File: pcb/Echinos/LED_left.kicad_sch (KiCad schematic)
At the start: 9 parts

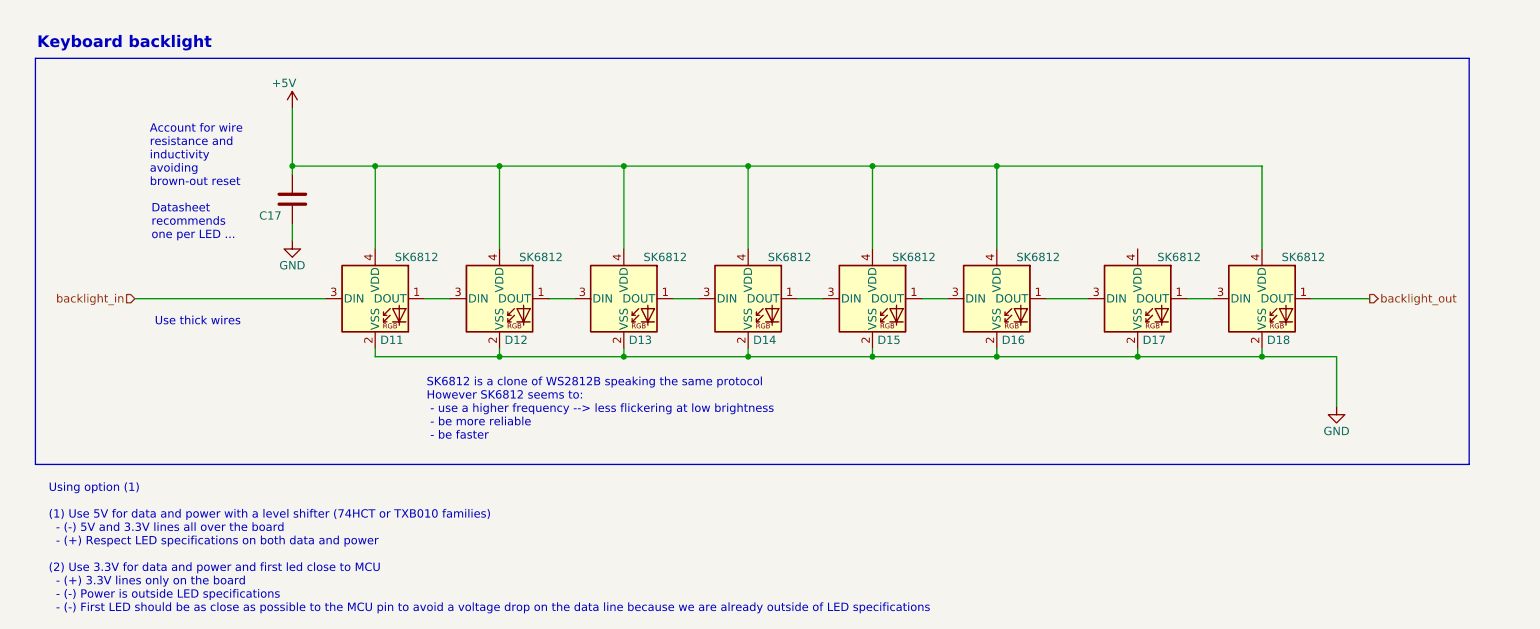
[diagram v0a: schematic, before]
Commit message: [PCB] - Save last state with Helios MCU board and gasket tabs on PCB.
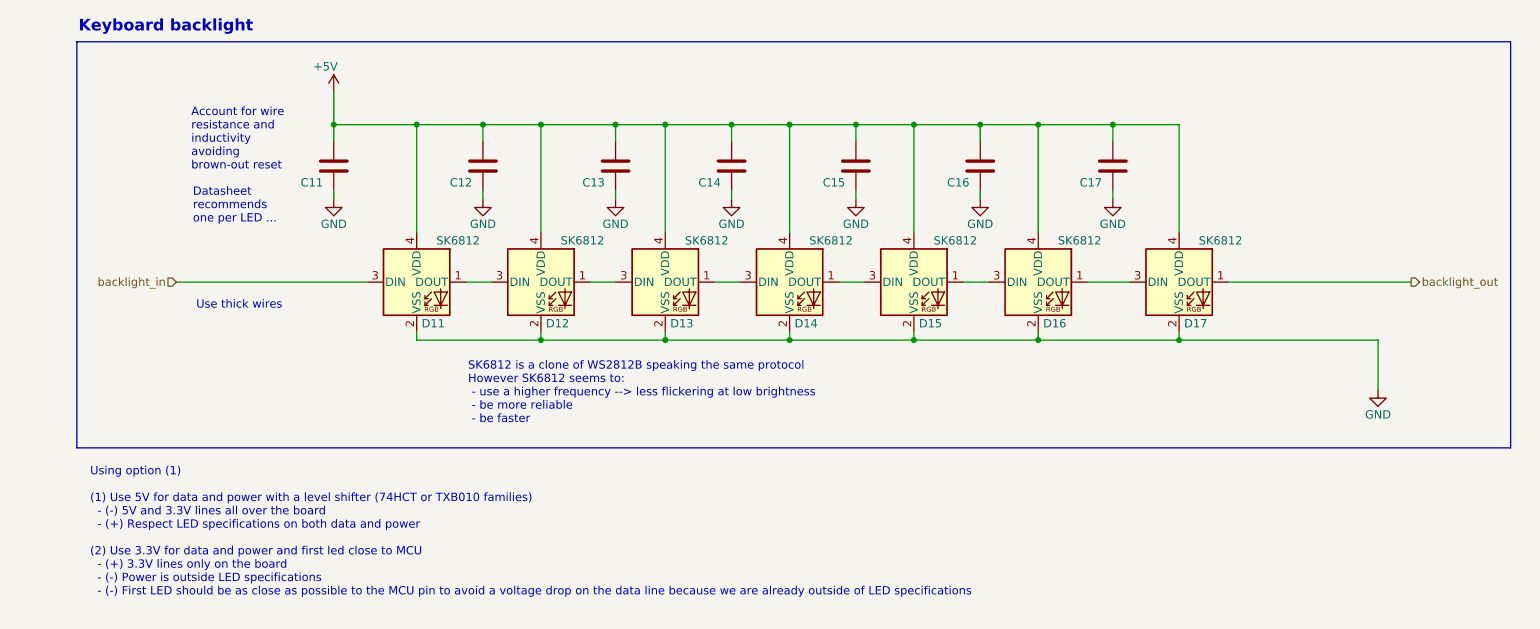
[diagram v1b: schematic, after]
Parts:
- removed D18: SK6812, LED_SMD:LED_SK6812_PLCC4_5.0x5.0mm_P3.2mm, symbol LED:SK6812MINI
- added C12, C13, C14, C15, C16, C17: 100nF, Capacitor_SMD:C_0805_2012Metric_Pad1.18x1.45mm_HandSolder, symbol Device:C
- C11: renamed from C17; footprint Capacitor_SMD:C_0402_1005Metric -> Capacitor_SMD:C_0805_2012Metric_Pad1.18x1.45mm_HandSolder; LCSC C52923 -> C1711
- D11, D12: LCSC (none) -> C7423110
- D13, D14, D15, D16, D17: LCSC C2886570 -> C7423110
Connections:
- net +5V: now also D17.4 (VDD), C12.1, C13.1, C14.1, C15.1, C16.1, C17.1
- net GND: now also C12.2, C13.2, C14.2, C15.2, C16.2, C17.2
- net backlight_out: now also D17.1 (DOUT)
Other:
- moved on the sheet: C11, D11, D12, D13, D14, D15, D16, D17

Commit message: [PCB] - Save last state with Helios MCU board.   - Fix LCSC part numbers (C11, F2)   - Fix pad numbering for SK6812 to match footprint and update PCB traces   - Use another LCSC part for LEDs that is available for economic assembly   - Remove jumpers from BOM (remove warning in JLCPCB)   - Add 180° rotation to FPCs (J1, J2, J3) to match selected part in JLCPCB manufacturing   - Add 180° rotation to LEDs to match selected part in JLCPCB manufacturing
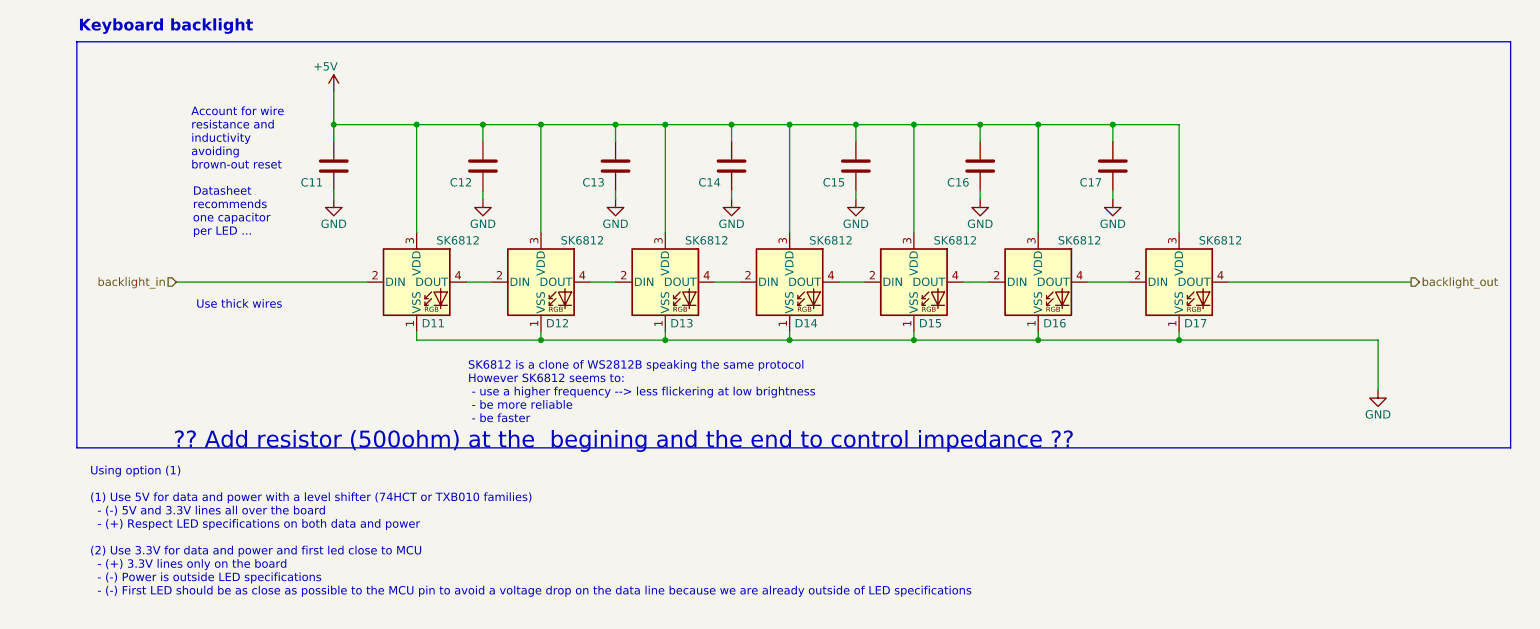
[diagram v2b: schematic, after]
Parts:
- C11: value 1µ -> 100nF
- D11, D12, D13, D14, D15, D16, D17: symbol LED:SK6812MINI -> LED:SK6812; FT Rotation Offset (none) -> 180; LCSC2 (none) -> C5378720
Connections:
- net +5V: now also D11.3 (VDD), D12.3 (VDD), D13.3 (VDD), D14.3 (VDD), D15.3 (VDD), D16.3 (VDD), D17.3 (VDD); no longer D11.4 (VDD), D12.4 (VDD), D13.4 (VDD), D14.4 (VDD), D15.4 (VDD), D16.4 (VDD), D17.4 (VDD)
- net GND: now also D11.1 (VSS), D12.1 (VSS), D13.1 (VSS), D14.1 (VSS), D15.1 (VSS), D16.1 (VSS), D17.1 (VSS); no longer D11.2 (VSS), D12.2 (VSS), D13.2 (VSS), D14.2 (VSS), D15.2 (VSS), D16.2 (VSS), D17.2 (VSS)
- net backlight_in: now also D11.2 (DIN); no longer D11.3 (DIN)
- net backlight_out: now also D17.4 (DOUT); no longer D17.1 (DOUT)
- new net: D13.4 (DOUT), D14.2 (DIN)
- new net: D14.4 (DOUT), D15.2 (DIN)
- new net: D11.4 (DOUT), D12.2 (DIN)
- new net: D16.4 (DOUT), D17.2 (DIN)
- new net: D15.4 (DOUT), D16.2 (DIN)
- new net: D12.4 (DOUT), D13.2 (DIN)
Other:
- note added: "?? Add resistor (500ohm) at the begining and the end to control impedance ??"
- note added: "Datasheet recommends one capacitor per LED ..."
- note removed: "Datasheet recommends one per LED ..."
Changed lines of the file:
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@@
+		)
+	)
+	(text "?? Add resistor (500ohm) at the  begining and the end to control impedance ??"
+		(exclude_from_sim no)
+		(at 106.68 84.074 0)
+		(effects
+			(font
+				(size 2.54 2.54)
+				(color 255 59 26 1)
+			)
 		)
 	)
@@
 		)
 	)
-	(text "Datasheet \nrecommends\none per LED ..."
-		(exclude_from_sim no)
-		(at 40.64 50.8 0)
+	(text "Datasheet \nrecommends\none capacitor \nper LED ..."
+		(exclude_from_sim no)
+		(at 40.64 52.832 0)
 		(effects
 			(font
@@
 	)
 	(symbol
-		(lib_id "LED:SK6812MINI")
+		(lib_id "LED:SK6812")
 		(at 132.08 59.69 0)
 		(unit 1)
@@
 			)
 		)
-		(property "Datasheet" "https://www.lcsc.com/datasheet/C7423110.pdf"
+		(property "Datasheet" "https://cdn-shop.adafruit.com/product-files/1138/SK6812+LED+datasheet+.pdf"
 			(at 134.62 69.215 0)
 			(effects
@@
 			)
 		)
-		(property "Description" ""
+		(property "Description" "RGB LED with integrated controller"
 			(at 132.08 59.69 0)
 			(effects
@@
 					(size 1.27 1.27)
 				)
+				(hide yes)
 			)
 		)
@@
 		)
 		(property "FT Position Offset" ""
+			(at 132.08 59.69 0)
+			(effects
+				(font
+					(size 1.27 1.27)
+				)
+				(hide yes)
+			)
+		)
+		(property "LCSC2" "C5378720 "
+			(at 132.08 59.69 0)
+			(effects
+				(font
+					(size 1.27 1.27)
+				)
+				(hide yes)
+			)
+		)
+		(property "FT Rotation Offset" "180"
 			(at 132.08 59.69 0)
 			(effects
@@
 	)
 	(symbol
-		(lib_id "LED:SK6812MINI")
+		(lib_id "LED:SK6812")
 		(at 74.93 59.69 0)
 		(unit 1)
@@
 			)
 		)
-		(property "Datasheet" "https://www.lcsc.com/datasheet/C7423110.pdf"
+		(property "Datasheet" "https://cdn-shop.adafruit.com/product-files/1138/SK6812+LED+datasheet+.pdf"
 			(at 77.47 69.215 0)
 			(effects
@@
 			)
 		)
-		(property "Description" ""
+		(property "Description" "RGB LED with integrated controller"
 			(at 74.93 59.69 0)
 			(effects
@@
 					(size 1.27 1.27)
 				)
+				(hide yes)
 			)
 		)
@@
 		)
 		(property "FT Position Offset" ""
+			(at 74.93 59.69 0)
+			(effects
+				(font
+					(size 1.27 1.27)
+				)
+				(hide yes)
+			)
+		)
+		(property "LCSC2" " C5378720 "
+			(at 74.93 59.69 0)
+			(effects
+				(font
+					(size 1.27 1.27)
+				)
+				(hide yes)
+			)
+		)
+		(property "FT Rotation Offset" "180"
 			(at 74.93 59.69 0)
 			(effects
@@
 	)
 	(symbol
-		(lib_id "LED:SK6812MINI")
+		(lib_id "LED:SK6812")
 		(at 191.77 59.69 0)
 		(unit 1)
@@
 			)
 		)
-		(property "Datasheet" "https://www.lcsc.com/datasheet/C7423110.pdf"
+		(property "Datasheet" "https://cdn-shop.adafruit.com/product-files/1138/SK6812+LED+datasheet+.pdf"
 			(at 194.31 69.215 0)
 			(effects
@@
 			)
 		)
-		(property "Description" ""
+		(property "Description" "RGB LED with integrated controller"
 			(at 191.77 59.69 0)
 			(effects
@@
 					(size 1.27 1.27)
 				)
+				(hide yes)
 			)
 		)
@@
 		)
 		(property "FT Position Offset" ""
+			(at 191.77 59.69 0)
+			(effects
+				(font
+					(size 1.27 1.27)
+				)
+				(hide yes)
+			)
+		)
+		(property "LCSC2" " C5378720 "
+			(at 191.77 59.69 0)
+			(effects
+				(font
+					(size 1.27 1.27)
+				)
+				(hide yes)
+			)
+		)
+		(property "FT Rotation Offset" "180"
 			(at 191.77 59.69 0)
 			(effects
@@
 			)
 		)
-		(property "Value" "1µ"
+		(property "Value" "100nF"
 			(at 63.5 44.45 0)
 			(effects
@@
 	)
 	(symbol
-		(lib_id "LED:SK6812MINI")
+		(lib_id "LED:SK6812")
 		(at 151.13 59.69 0)
 		(unit 1)
@@
 			)
 		)
-		(property "Datasheet" "https://www.lcsc.com/datasheet/C7423110.pdf"
+		(property "Datasheet" "https://cdn-shop.adafruit.com/product-files/1138/SK6812+LED+datasheet+.pdf"
 			(at 153.67 69.215 0)
 			(effects
@@
 			)
 		)
-		(property "Description" ""
+		(property "Description" "RGB LED with integrated controller"
 			(at 151.13 59.69 0)
 			(effects
@@
 					(size 1.27 1.27)
 				)
+				(hide yes)
 			)
 		)
@@
 		)
 		(property "FT Position Offset" ""
+			(at 151.13 59.69 0)
+			(effects
+				(font
+					(size 1.27 1.27)
+				)
+				(hide yes)
+			)
+		)
+		(property "LCSC2" " C5378720 "
+			(at 151.13 59.69 0)
+			(effects
+				(font
+					(size 1.27 1.27)
+				)
+				(hide yes)
+			)
+		)
+		(property "FT Rotation Offset" "180"
 			(at 151.13 59.69 0)
 			(effects
@@
 	)
 	(symbol
-		(lib_id "LED:SK6812MINI")
+		(lib_id "LED:SK6812")
 		(at 93.98 59.69 0)
 		(unit 1)
@@
 			)
 		)
-		(property "Datasheet" "https://www.lcsc.com/datasheet/C7423110.pdf"
+		(property "Datasheet" "https://cdn-shop.adafruit.com/product-files/1138/SK6812+LED+datasheet+.pdf"
 			(at 96.52 69.215 0)
 			(effects
@@
 			)
 		)
-		(property "Description" ""
+		(property "Description" "RGB LED with integrated controller"
 			(at 93.98 59.69 0)
 			(effects
@@
 					(size 1.27 1.27)
 				)
+				(hide yes)
 			)
 		)
@@
 		)
 		(property "FT Position Offset" ""
+			(at 93.98 59.69 0)
+			(effects
+				(font
+					(size 1.27 1.27)
+				)
+				(hide yes)
+			)
+		)
+		(property "LCSC2" "C5378720 "
+			(at 93.98 59.69 0)
+			(effects
+				(font
+					(size 1.27 1.27)
+				)
+				(hide yes)
+			)
+		)
+		(property "FT Rotation Offset" "180"
 			(at 93.98 59.69 0)
 			(effects
@@
 	)
 	(symbol
-		(lib_id "LED:SK6812MINI")
+		(lib_id "LED:SK6812")
 		(at 113.03 59.69 0)
 		(unit 1)
@@
 			)
 		)
-		(property "Datasheet" "https://www.lcsc.com/datasheet/C7423110.pdf"
+		(property "Datasheet" "https://cdn-shop.adafruit.com/product-files/1138/SK6812+LED+datasheet+.pdf"
 			(at 115.57 69.215 0)
 			(effects
@@
 			)
 		)
-		(property "Description" ""
+		(property "Description" "RGB LED with integrated controller"
 			(at 113.03 59.69 0)
 			(effects
@@
 					(size 1.27 1.27)
 				)
+				(hide yes)
 			)
 		)
@@
 		)
 		(property "FT Position Offset" ""
+			(at 113.03 59.69 0)
+			(effects
+				(font
+					(size 1.27 1.27)
+				)
+				(hide yes)
+			)
+		)
+		(property "LCSC2" " C5378720 "
+			(at 113.03 59.69 0)
+			(effects
+				(font
+					(size 1.27 1.27)
+				)
+				(hide yes)
+			)
+		)
+		(property "FT Rotation Offset" "180"
 			(at 113.03 59.69 0)
 			(effects
@@
 	)
 	(symbol
-		(lib_id "LED:SK6812MINI")
+		(lib_id "LED:SK6812")
 		(at 170.18 59.69 0)
 		(unit 1)
@@
 			)
 		)
-		(property "Datasheet" "https://www.lcsc.com/datasheet/C7423110.pdf"
+		(property "Datasheet" "https://cdn-shop.adafruit.com/product-files/1138/SK6812+LED+datasheet+.pdf"
 			(at 172.72 69.215 0)
 			(effects
@@
 			)
 		)
-		(property "Description" ""
+		(property "Description" "RGB LED with integrated controller"
 			(at 170.18 59.69 0)
 			(effects
@@
 					(size 1.27 1.27)
 				)
+				(hide yes)
 			)
 		)
@@
 			(at 170.18 59.69 0)
 			(effects
+				(font
+					(size 1.27 1.27)
+				)
+				(hide yes)
+			)
+		)
+		(property "LCSC2" "C5378720 "
+			(at 170.18 59.69 0)
+			(effects
+				(font
+					(size 1.27 1.27)
+				)
+				(hide yes)
+			)
+		)
+		(property "FT Rotation Offset" "180"
+			(at 170.18 59.69 0)
+			(effects

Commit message: [PCB] - Save last state with on board RP2040.   - Clean schematics   - Fix flash capacitor value   - Fix flash schema to match all footprint pins   - Pass ERC (schema and pcb)   - Select missing LCSC components (USBC/B, buttons, vik connector)   - Add more margin to lateral pads in USB B footprint   - Improve top plane grounding under switches   - Adjust orientation and position to match JLCPCB   - Clean unused fields in schematics   - Add VIK connector footprint to lib (updated to match more models)   - Harmonization of footprints packaging for caps and resistors (either 0805 or 0402)   - Check availability and correctness of all parts   - Fix space in fields (was LCSC2 on leds)
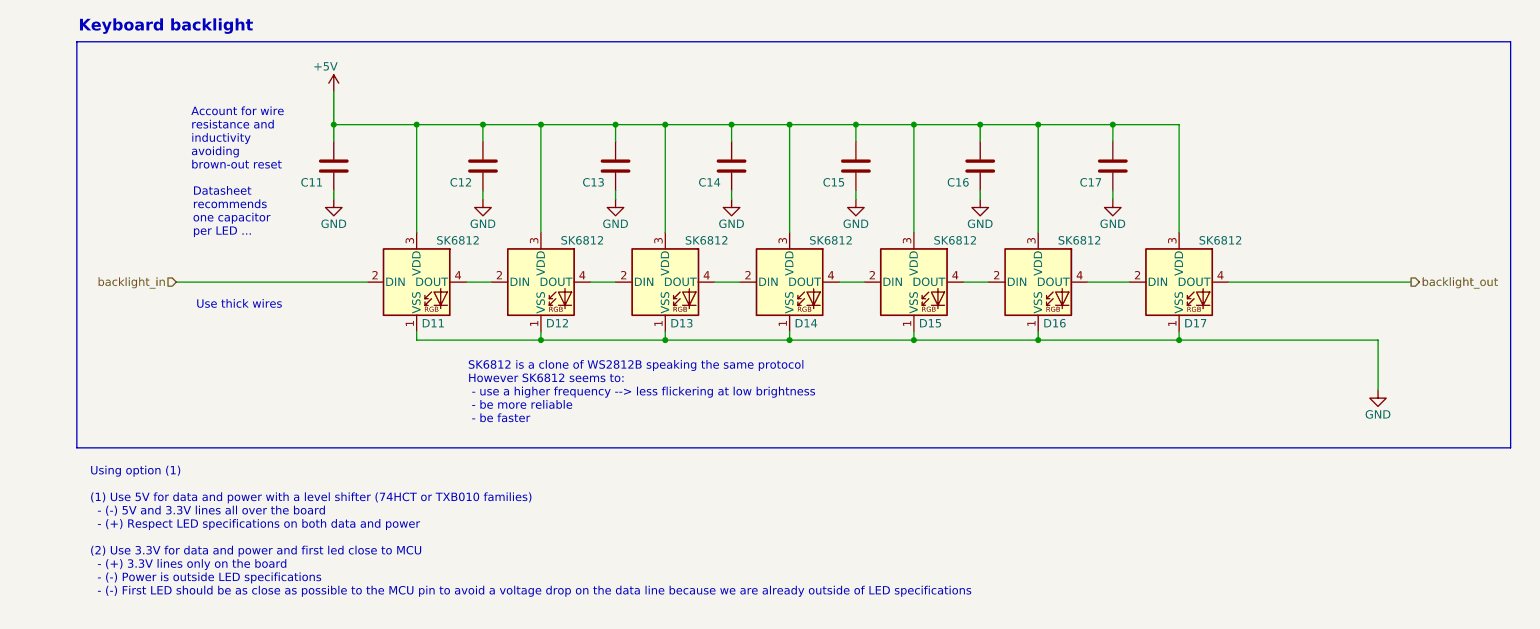
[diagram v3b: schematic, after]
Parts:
- C11, C12, C13, C14, C15, C16, C17: value 100nF -> 100n; footprint Capacitor_SMD:C_0805_2012Metric_Pad1.18x1.45mm_HandSolder -> Capacitor_SMD:C_0805_2012Metric
- D11, D12, D13, D14, D15, D16, D17: LCSC2 C5378720 -> C5378720
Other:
- note removed: "?? Add resistor (500ohm) at the begining and the end to control impedance ??"
- title: (none) -> Backlight
